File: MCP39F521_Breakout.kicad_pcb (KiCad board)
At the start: 2 copper layers, 35.6 x 27.9 mm, 37 parts, among them J11 Conn_01x10, J2 Conn_01x01, J4 Conn_01x01, J5 Conn_01x01, U1 MCP39F521, U2 MCP9700AT-ETT, Y1 Crystal

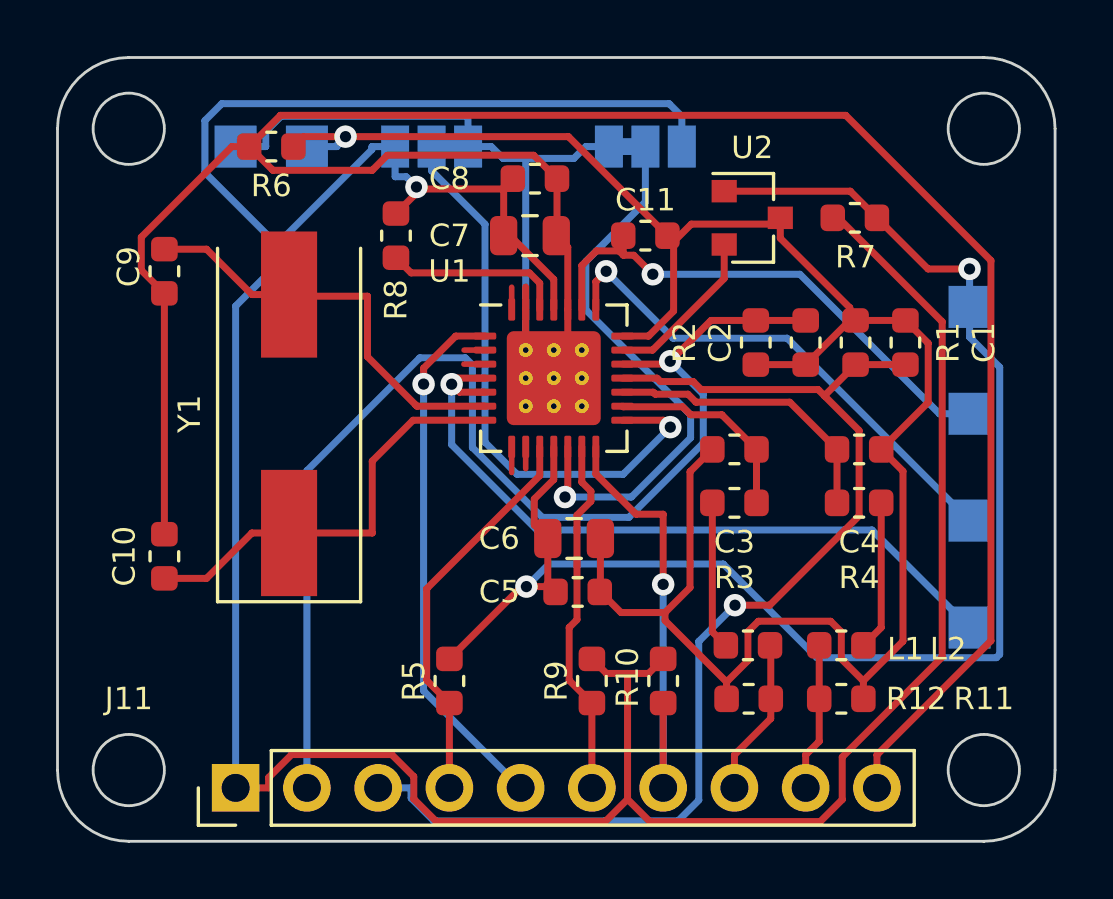
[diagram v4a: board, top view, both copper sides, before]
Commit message: Ground planes and vias
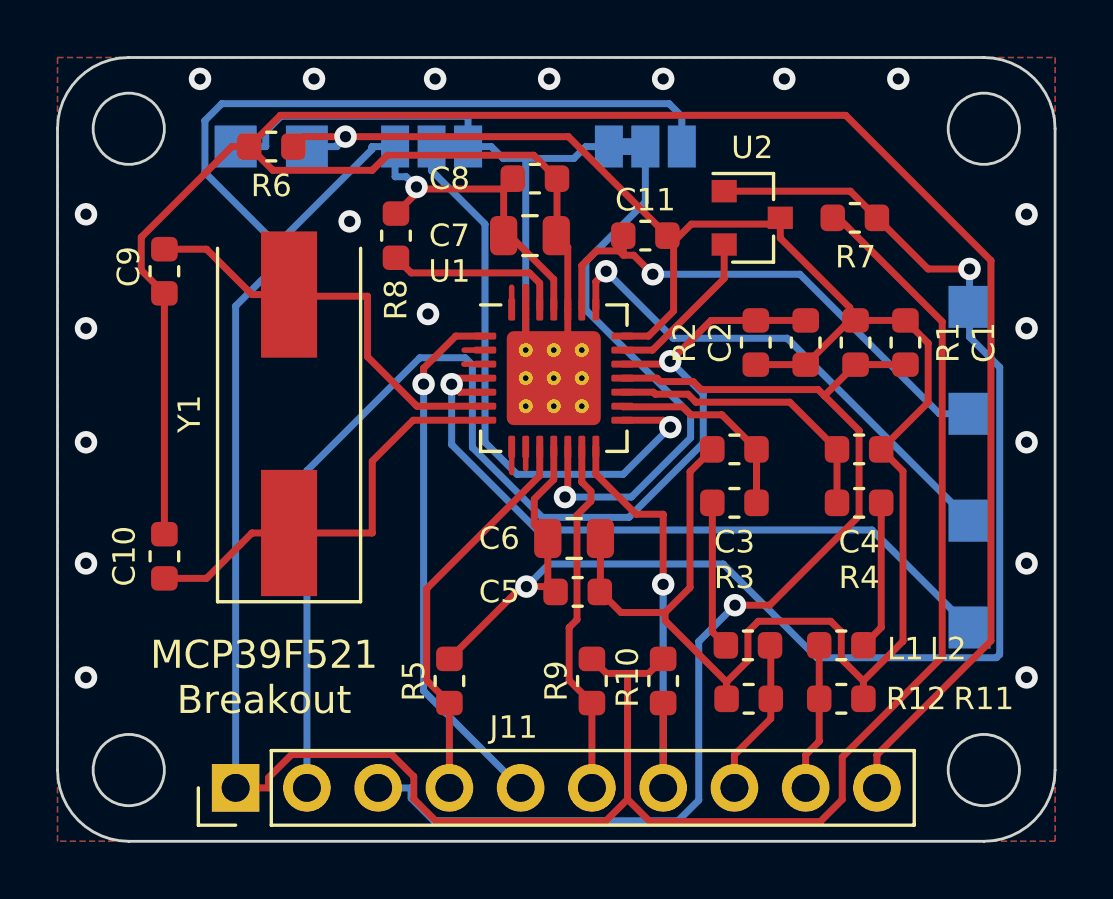
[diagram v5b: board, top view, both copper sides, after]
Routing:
- net NC: track 0.00 -> 3.98 mm
- net (no net): track 3.98 -> 0.00 mm
- net GNDD: vias 0 -> 19
- added copper zone on B.Cu, net GNDD
- added copper zone on F.Cu, net GNDD
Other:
- board text added: "MCP39F521 Breakout"
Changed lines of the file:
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@@
     )
   )
-  (net 0 "")
+  (net 0 "NC")
   (net 1 "VN")
   (net 2 "VP")
@@
     (property "Sheet name" "")
     (attr through_hole)
-    (fp_text reference "J11" (at 3.175 -3.81 180) (layer "F.SilkS")
+    (fp_text reference "J11" (at 2.159 9.906 180) (layer "F.SilkS")
       (effects (font (size 0.8 0.8) (thickness 0.2)))
     )
@@
   (gr_line (start 114.3 99.06) (end 114.3 121.92) (layer "Edge.Cuts") (width 0.1))
   (gr_line (start 116.84 96.52) (end 147.32 96.52) (layer "Edge.Cuts") (width 0.1))
+  (gr_text "MCP39F521\nBreakout" (at 121.666 118.618) (layer "F.SilkS")
+    (effects (font (size 1 1) (thickness 0.25)))
+  )
   (segment (start 130.49 104.709) (end 130.49 105.5) (width 0.2) (layer "F.Cu") (net 0))
   (segment (start 130.49 110.4) (end 130.49 111.313) (width 0.2) (layer "F.Cu") (net 0))
@@
   (segment (start 117.2859 104.1034) (end 117.2859 102.9253) (width 0.25) (layer "F.Cu") (net 18))
   (segment (start 121.1325 99.695) (end 122.2462 98.5813) (width 0.25) (layer "F.Cu") (net 18))
+  (via (at 131.826 97.282) (size 0.8) (drill 0.4) (layers "F.Cu" "B.Cu") (net 18))
+  (via (at 148.844 114.554) (size 0.8) (drill 0.4) (layers "F.Cu" "B.Cu") (net 18))
+  (via (at 115.316 114.554) (size 0.8) (drill 0.4) (layers "F.Cu" "B.Cu") (net 18))
+  (via (at 115.316 102.108) (size 0.8) (drill 0.4) (layers "F.Cu" "B.Cu") (net 18))
+  (via (at 115.316 106.172) (size 0.8) (drill 0.4) (layers "F.Cu" "B.Cu") (net 18))
+  (via (at 148.844 102.108) (size 0.8) (drill 0.4) (layers "F.Cu" "B.Cu") (net 18))
+  (via (at 140.208 97.282) (size 0.8) (drill 0.4) (layers "F.Cu" "B.Cu") (net 18))
+  (via (at 127.762 97.282) (size 0.8) (drill 0.4) (layers "F.Cu" "B.Cu") (net 18))
+  (via (at 127.508 105.664) (size 0.8) (drill 0.4) (layers "F.Cu" "B.Cu") (net 18))
+  (via (at 148.844 106.172) (size 0.8) (drill 0.4) (layers "F.Cu" "B.Cu") (net 18))
+  (via (at 148.844 118.618) (size 0.8) (drill 0.4) (layers "F.Cu" "B.Cu") (net 18))
+  (via (at 115.316 110.236) (size 0.8) (drill 0.4) (layers "F.Cu" "B.Cu") (net 18))
+  (via (at 124.714 102.362) (size 0.8) (drill 0.4) (layers "F.Cu" "B.Cu") (net 18))
+  (via (at 144.272 97.282) (size 0.8) (drill 0.4) (layers "F.Cu" "B.Cu") (net 18))
+  (via (at 115.316 118.618) (size 0.8) (drill 0.4) (layers "F.Cu" "B.Cu") (net 18))
+  (via (at 123.444 97.282) (size 0.8) (drill 0.4) (layers "F.Cu" "B.Cu") (net 18))
+  (via (at 135.89 97.282) (size 0.8) (drill 0.4) (layers "F.Cu" "B.Cu") (net 18))
+  (via (at 119.38 97.282) (size 0.8) (drill 0.4) (layers "F.Cu" "B.Cu") (net 18))
+  (via (at 148.844 110.236) (size 0.8) (drill 0.4) (layers "F.Cu" "B.Cu") (net 18))
   (segment (start 132.707 100.1177) (end 133.1297 99.695) (width 0.25) (layer "B.Cu") (net 18))
   (segment (start 120.65 99.695) (end 121.7253 99.695) (width 0.25) (layer "B.Cu") (net 18))
@@
   (segment (start 143.335403 113.363403) (end 131.394581 113.363403) (width 0.25) (layer "B.Cu") (net 25))
   (segment (start 131.394581 113.363403) (end 128.349971 110.318793) (width 0.25) (layer "B.Cu") (net 25))
+  (zone (net 18) (net_name "GNDD") (layers F&B.Cu) (hatch edge 0.508)
+    (connect_pads (clearance 0.508))
+    (min_thickness 0.254) (filled_areas_thickness no)
+    (fill yes (thermal_gap 0.508) (thermal_bridge_width 0.508))
+    (polygon
+      (pts
+        (xy 149.86 124.46)
+        (xy 114.3 124.46)
+        (xy 114.3 96.52)
+        (xy 149.86 96.52)
+      )
+    )
+  )
 )

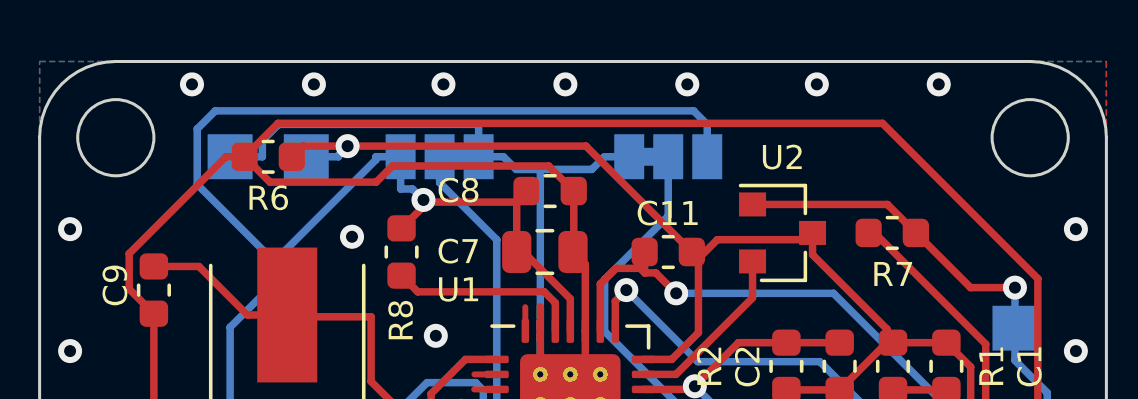
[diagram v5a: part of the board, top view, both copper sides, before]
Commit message: Clean up silk screen
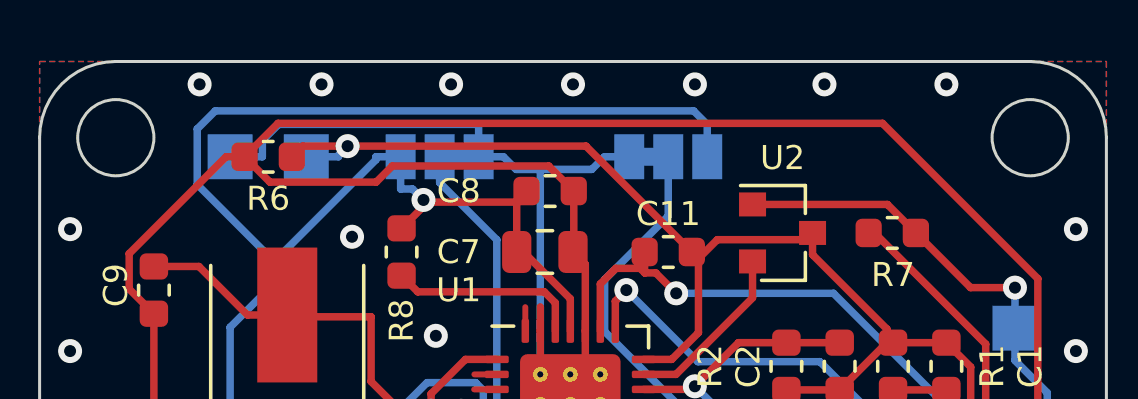
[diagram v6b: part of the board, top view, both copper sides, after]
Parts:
- added LOGO1: Logo_Open_Hardware_Small, Symbol:OSHW-Logo2_7.3x6mm_SilkScreen, B.Cu at (131.6, 113.8)
- added LOGO2: LOGO, Whatnick_logo:Whatnick_logo, B.Cu at (120.9, 110.7)
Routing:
- net NC: track 3.98 -> 0.00 mm
- net (no net): track 0.00 -> 3.98 mm
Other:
- board text added: "3V3"
- board text added: "EVENT"
- board text added: "GNDD"
- board text added: "IN"
- board text added: "IP"
- board text added: "SCL"
- board text added: "SDA"
- board text added: "VN"
- board text added: "VP"
- board text added: "by Tisham Dhar http://whatnick.com v0.1 26/12/2020"
- board text added: "~RESET"

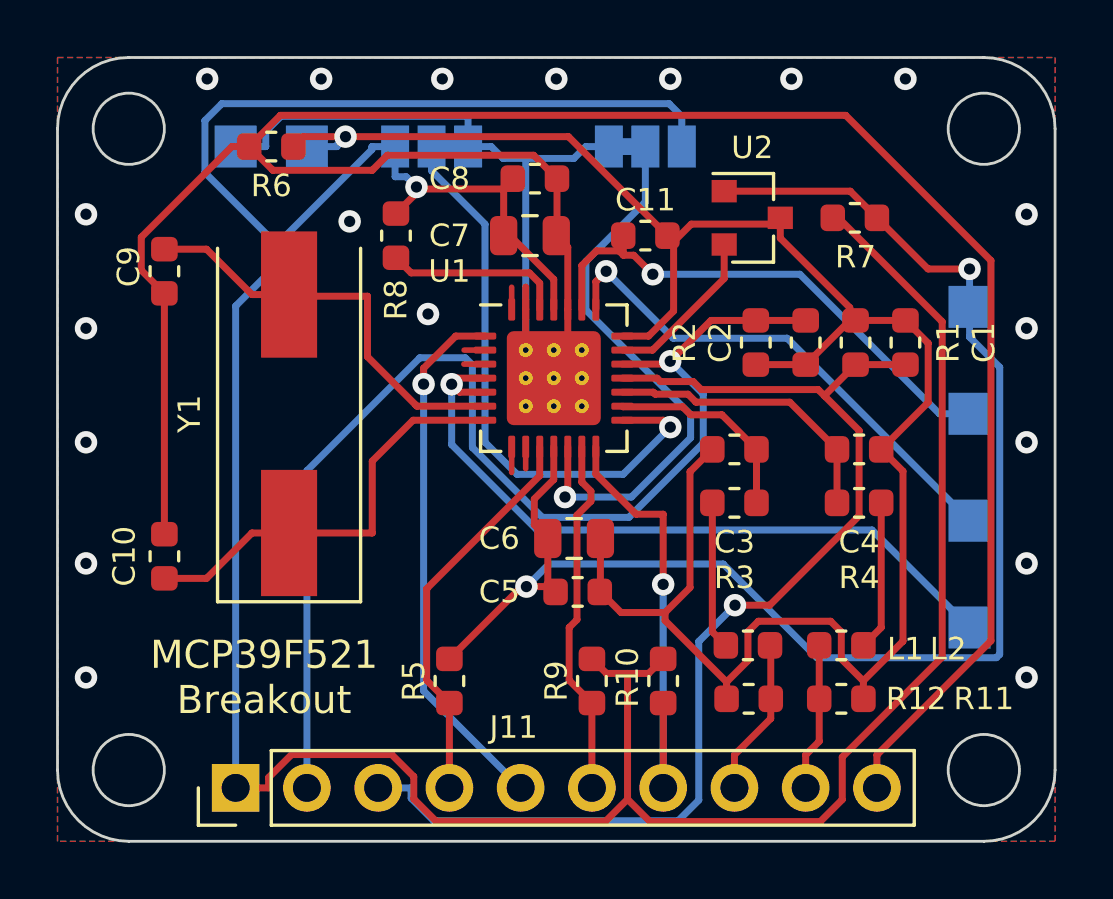
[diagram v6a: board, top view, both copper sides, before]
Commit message: Create gerbers and swap to non-via footprint
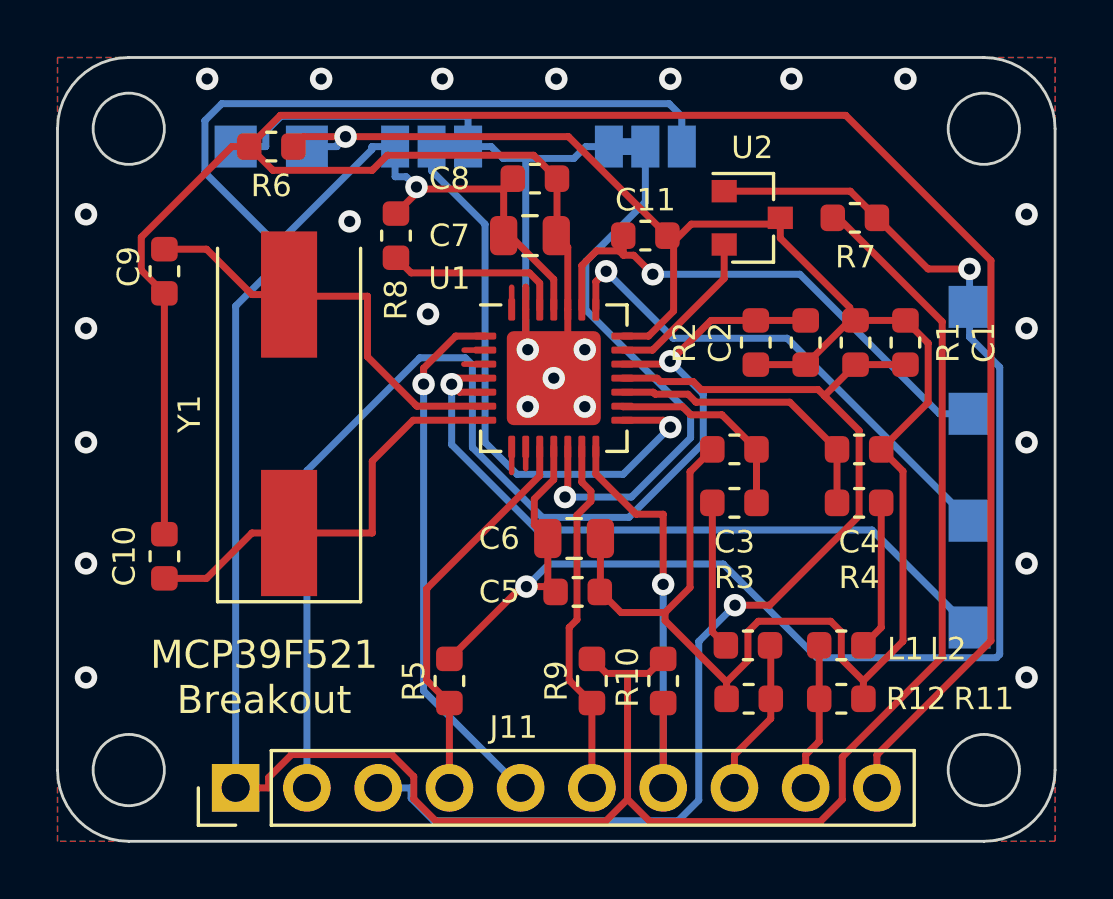
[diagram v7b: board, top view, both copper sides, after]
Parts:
- U1: footprint Package_DFN_QFN:QFN-28-1EP_5x5mm_P0.5mm_EP3.35x3.35mm_ThermalVias -> Package_DFN_QFN:QFN-28-1EP_5x5mm_P0.5mm_EP3.35x3.35mm
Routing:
- net GNDD: vias 19 -> 24
